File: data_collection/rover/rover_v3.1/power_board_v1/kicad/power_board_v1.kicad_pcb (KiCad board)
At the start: 2 copper layers, 90 x 65 mm, 131 parts, among them J1 XT60_BATT, J10 from Pi USB2, J11 UPDI prog (UPDI/3V3/GND), J12 XT30 fallback pads, J2 PANEL_SW, J3 USB4105-GF-A (TH shell), J4 USB_A radio1, J5 USB_A radio2, J6 AUX 5V 2A, J7 PI GPIO harness, J8 AUX_CTL out (JST-GH), J9 from Pi USB1, Q2 CSD18543Q3A diode, Q3 CSD18543Q3A switch, U1 LM5145 rail A, U2 LM5145 rail B, U3 ATtiny816 (VQFN), U4 LM74800-Q1, U5 INA226 (addr 0x40), U6 TPS7A1633 3V3 60V LDO, U7 TPS2553 1.7A, U8 TPS2553 1.7A, U9 AP2112K-3.3 (switched)

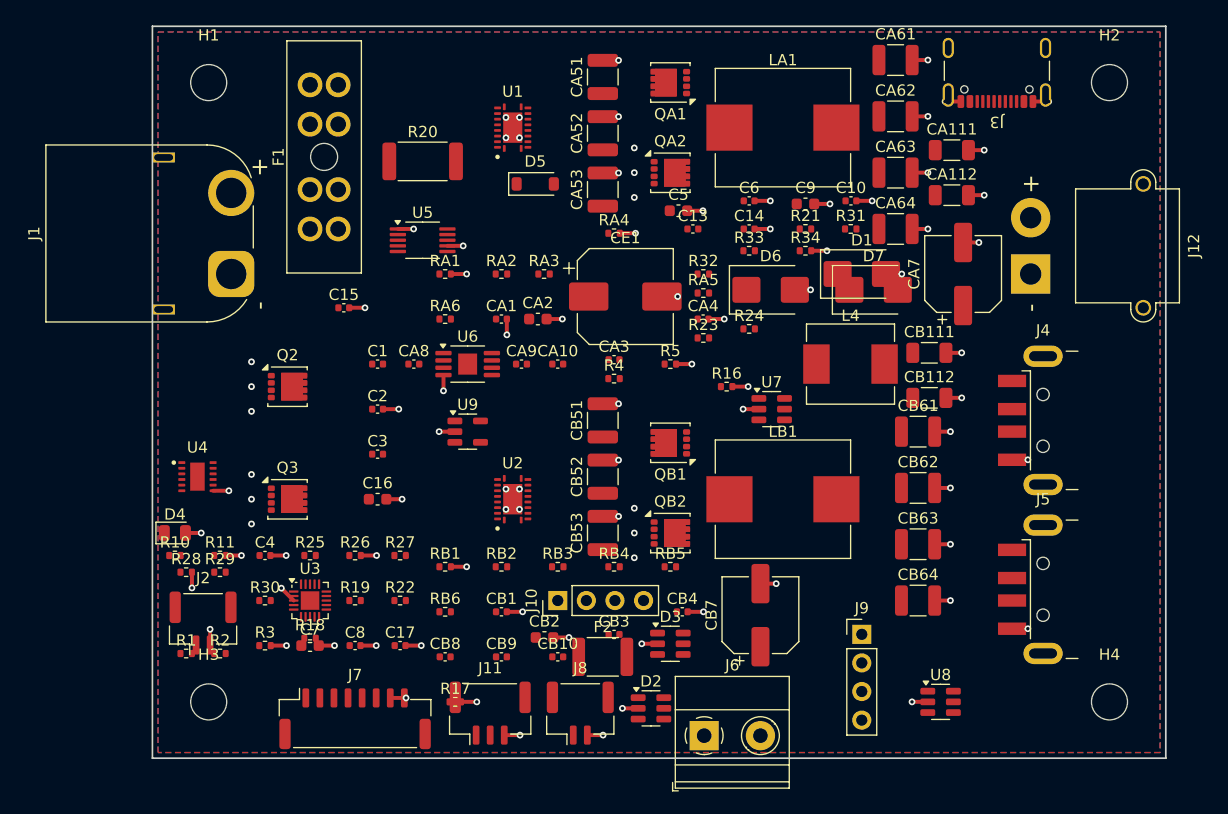
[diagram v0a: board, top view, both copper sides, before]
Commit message: 4-layer board (In1 GND plane, In2 power pours) + custom maze router: 362 segs + 327 vias, exact-rect clearance model, A* 2-layer maze; freerouting version matrix exhausted+documented; ~110 pairs remain for interactive pass; AUDIT PASS, baseline updated
Co-Authored-By: Claude Fable 5 <noreply@anthropic.com>
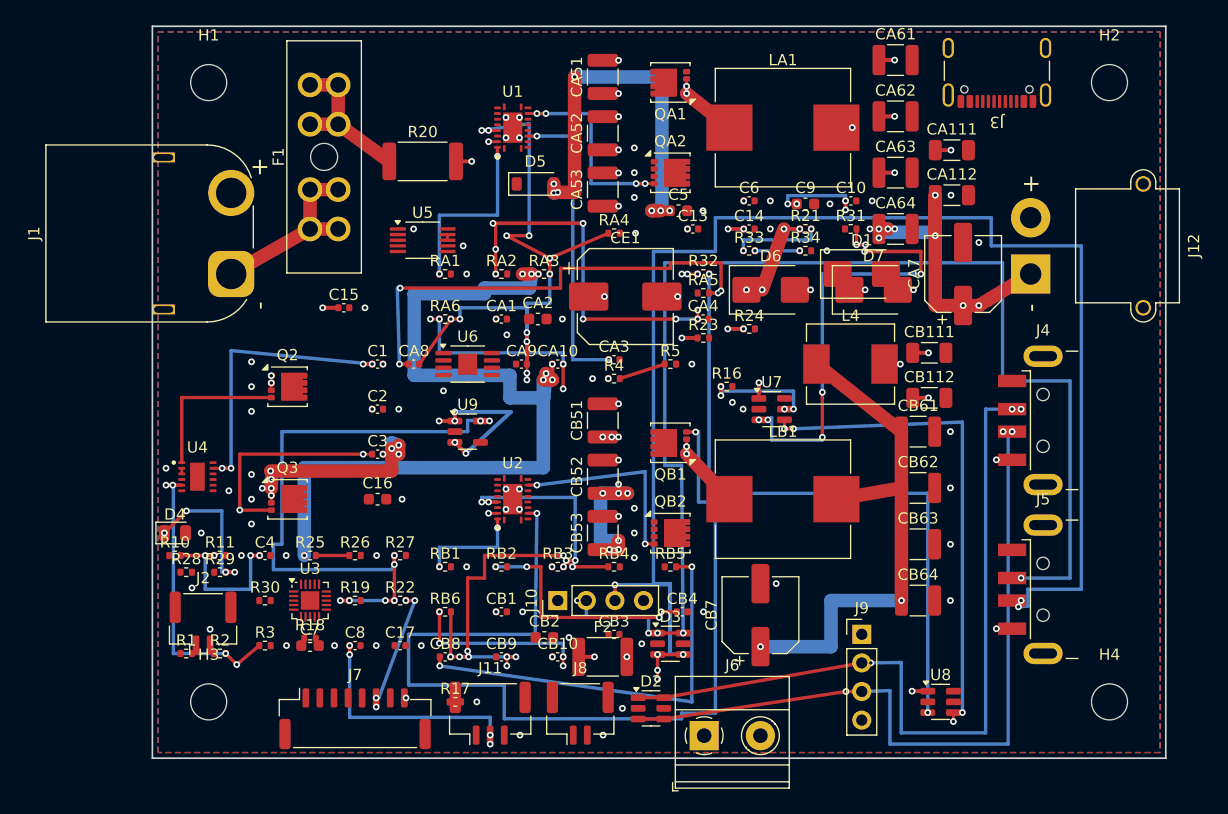
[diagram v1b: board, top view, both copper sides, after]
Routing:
- net D2_P: track 0.00 -> 138.3 mm, vias 0 -> 8
- net 5V_A: track 0.00 -> 123.6 mm, vias 0 -> 30
- net D2_N: track 0.00 -> 115.0 mm, vias 0 -> 6
- net GND: track 99.6 -> 0.00 mm, vias 91 -> 77
- net HO_B: track 0.00 -> 85.6 mm, vias 0 -> 2
- net D1_N: track 0.00 -> 70.1 mm, vias 0 -> 4
- net D1_P: track 0.00 -> 66.7 mm, vias 0 -> 4
- net 3V3_SW: track 0.00 -> 63.4 mm, vias 0 -> 12
- net FB_A: track 0.00 -> 58.9 mm, vias 0 -> 12
- net EN_USB2: track 0.00 -> 58.4 mm, vias 0 -> 2
- net FB_B: track 0.00 -> 51.0 mm, vias 0 -> 14
- net 5VB_PRE: track 0.00 -> 47.1 mm, vias 0 -> 4
- net EN_USB1: track 0.00 -> 45.9 mm, vias 0 -> 8
- net FAULT_USB: track 0.00 -> 44.0 mm, vias 0 -> 4
- net CX_A: track 0.00 -> 41.9 mm, vias 0 -> 4
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- added copper zone on In2.Cu, net 5V_A
- added copper zone on In2.Cu, net 5V_B
- added copper zone on In1.Cu, net GND
- added copper zone on In2.Cu, net VBATT_S
- added copper zone on In2.Cu, net VSW
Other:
- copper layers 2 -> 4
